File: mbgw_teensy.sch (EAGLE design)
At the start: 39 parts, among them IC1 MAX481CSA, Q1 MOSFET-N2N7002, Q2 MOSFET-N2N7002, Q3 MOSFET-N2N7002

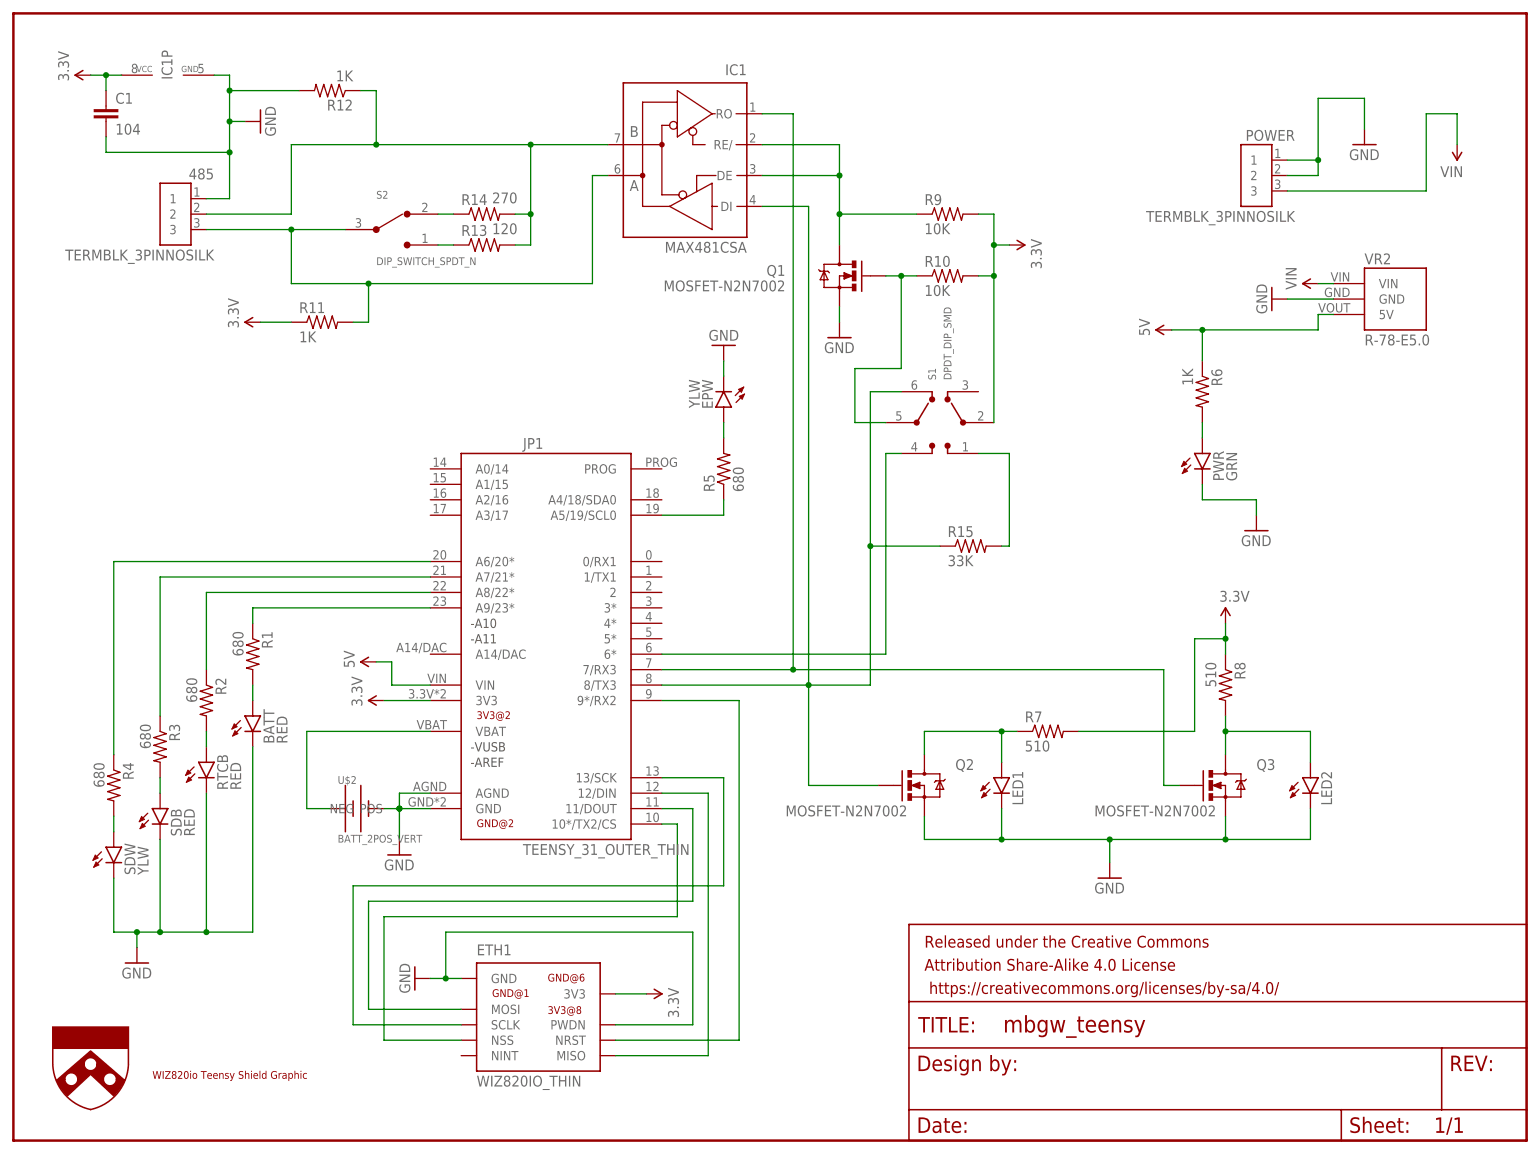
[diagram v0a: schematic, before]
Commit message: 3/16/17, board with software switches for term resistor and tx/p6 control
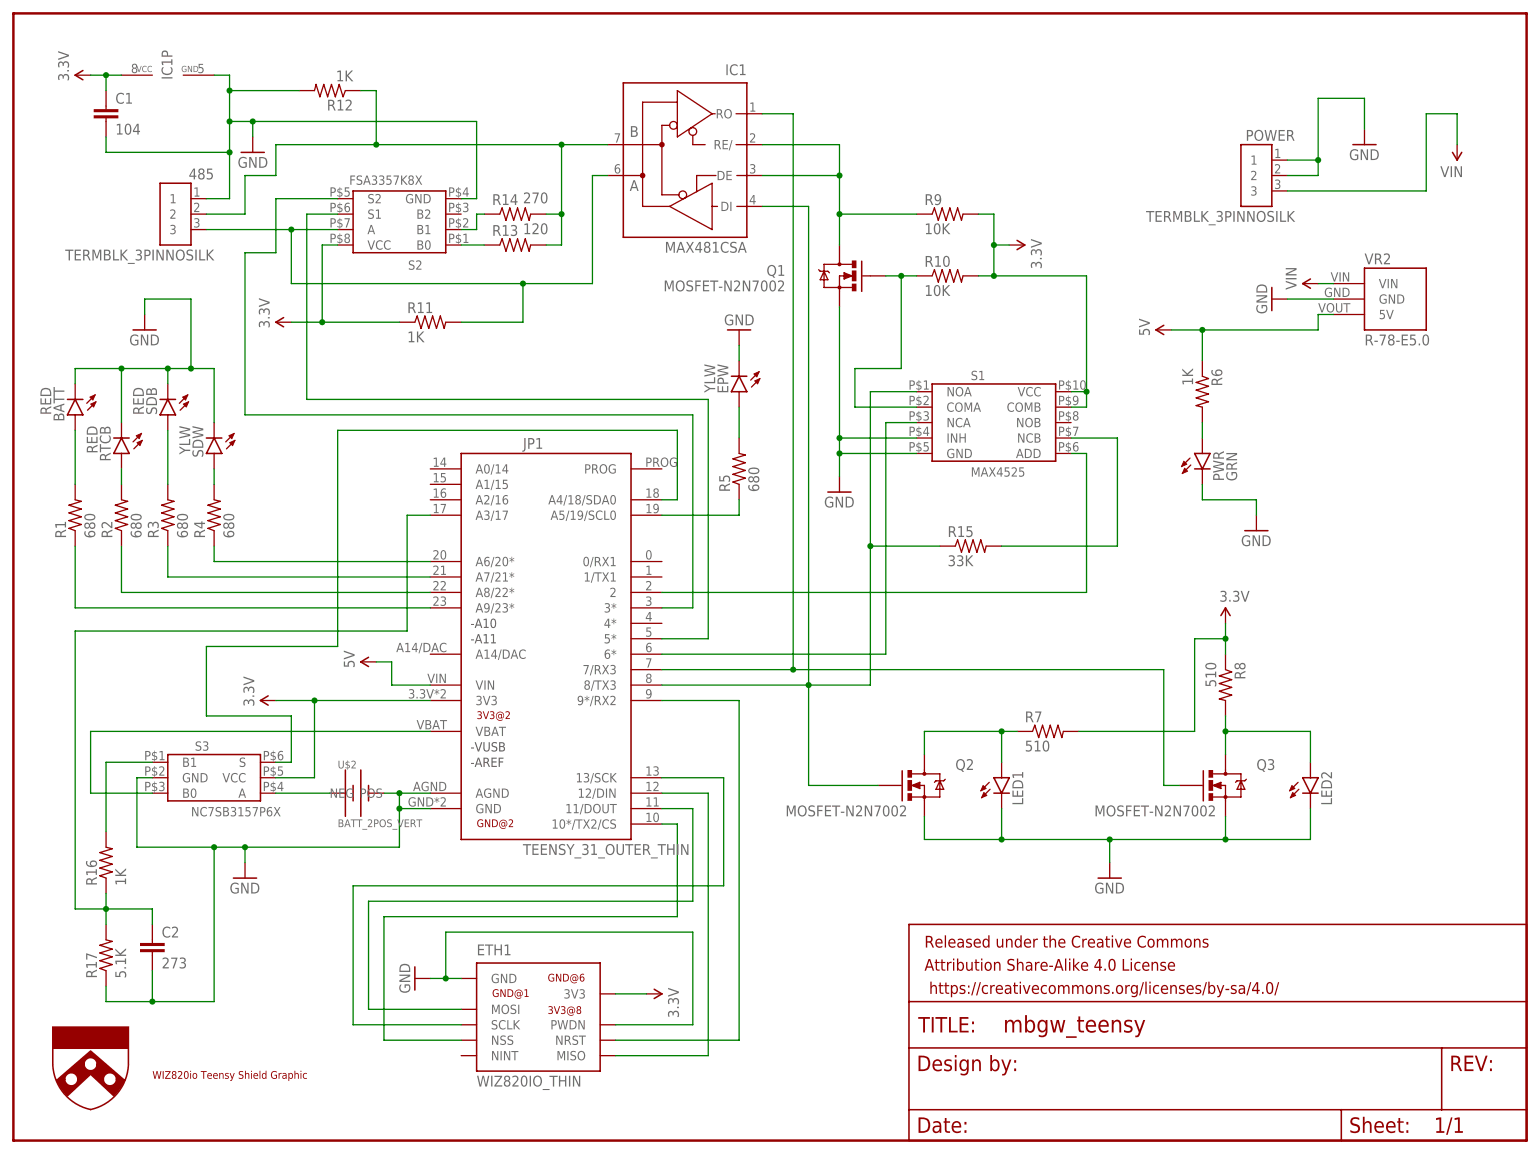
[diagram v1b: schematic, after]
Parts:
- added C2: 273, SparkFun-Capacitors:CAP0603-CAP
- added R16: 1K, SparkFun-Resistors:RESISTOR0603
- added R17: 5.1K, SparkFun-Resistors:RESISTOR0603
- added S3: NC7SB3157P6X, UPenn:NC7SB3157P6X
- S1: value DPDT_DIP_SMD -> MAX4525; device UPenn:DPDT_DIP_SMD -> UPenn:MAX4525
- S2: value DIP_SWITCH_SPDT_N -> FSA3357K8X; device UPenn:DIP_SWITCH_SPDT_N -> UPenn:FSA3357K8X
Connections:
- new net N$30: R14.1, S2.B1
- new net N$31: JP1.3*, S2.S2
- new net N$32: JP1.2, S1.ADD
- new net N$33: JP1.VBAT, S3.B0
- new net N$35: C2.1, JP1.A3/17, R16.1, R17.2
- new net N$37: R16.2, S3.B1
- new net N$38: JP1.A4/18/SDA0, S3.S
- net 3.3V: now also S1.COMB, S1.VCC, S2.VCC, S3.VCC; no longer S1.<2
- net GND: now also C2.2, R17.1, S1.GND, S1.INH, S2.GND, S3.GND
- net N$1: now also R15.2, S1.NCB; no longer R14.1, S2.2
- net N$12: now also S2.B0; no longer S2.1
- net N$15: now also JP1.5*, S2.S1; no longer R15.2, S1.<1
- net N$17: now also S1.NOA; no longer S1.6>
- net N$2: now also S1.NCA; no longer S1.4>
- net N$25: now also S2.A; no longer S2.3
- net N$26: now also S1.COMA; no longer S1.5>
- net N$3: now also S3.A; no longer JP1.VBAT
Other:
- moved on the sheet: BATT, EPW, R1, R11, R13, R14, R2, R3, R4, R5, RTCB, SDB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

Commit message: 3/20/17, continue adjusting for stretched board
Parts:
- added MEM1: RM25C512CSOIC, UPenn:RM25C512CSOIC
- added R18: 180, SparkFun-Resistors:RESISTOR0603
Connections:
- new net N$34: R18.1, S2.B2
- net 3.3V: now also MEM1.!HOLD!, MEM1.!WP!, MEM1.VCC
- net GND: now also MEM1.GND
- net N$13: now also R18.2
- net N$6: now also MEM1.SDI
- net N$7: now also MEM1.SDO
- net N$8: now also MEM1.SCK
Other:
- moved on the sheet: LED1, LED2, Q2, Q3, R13, R14, R15, R7, S1

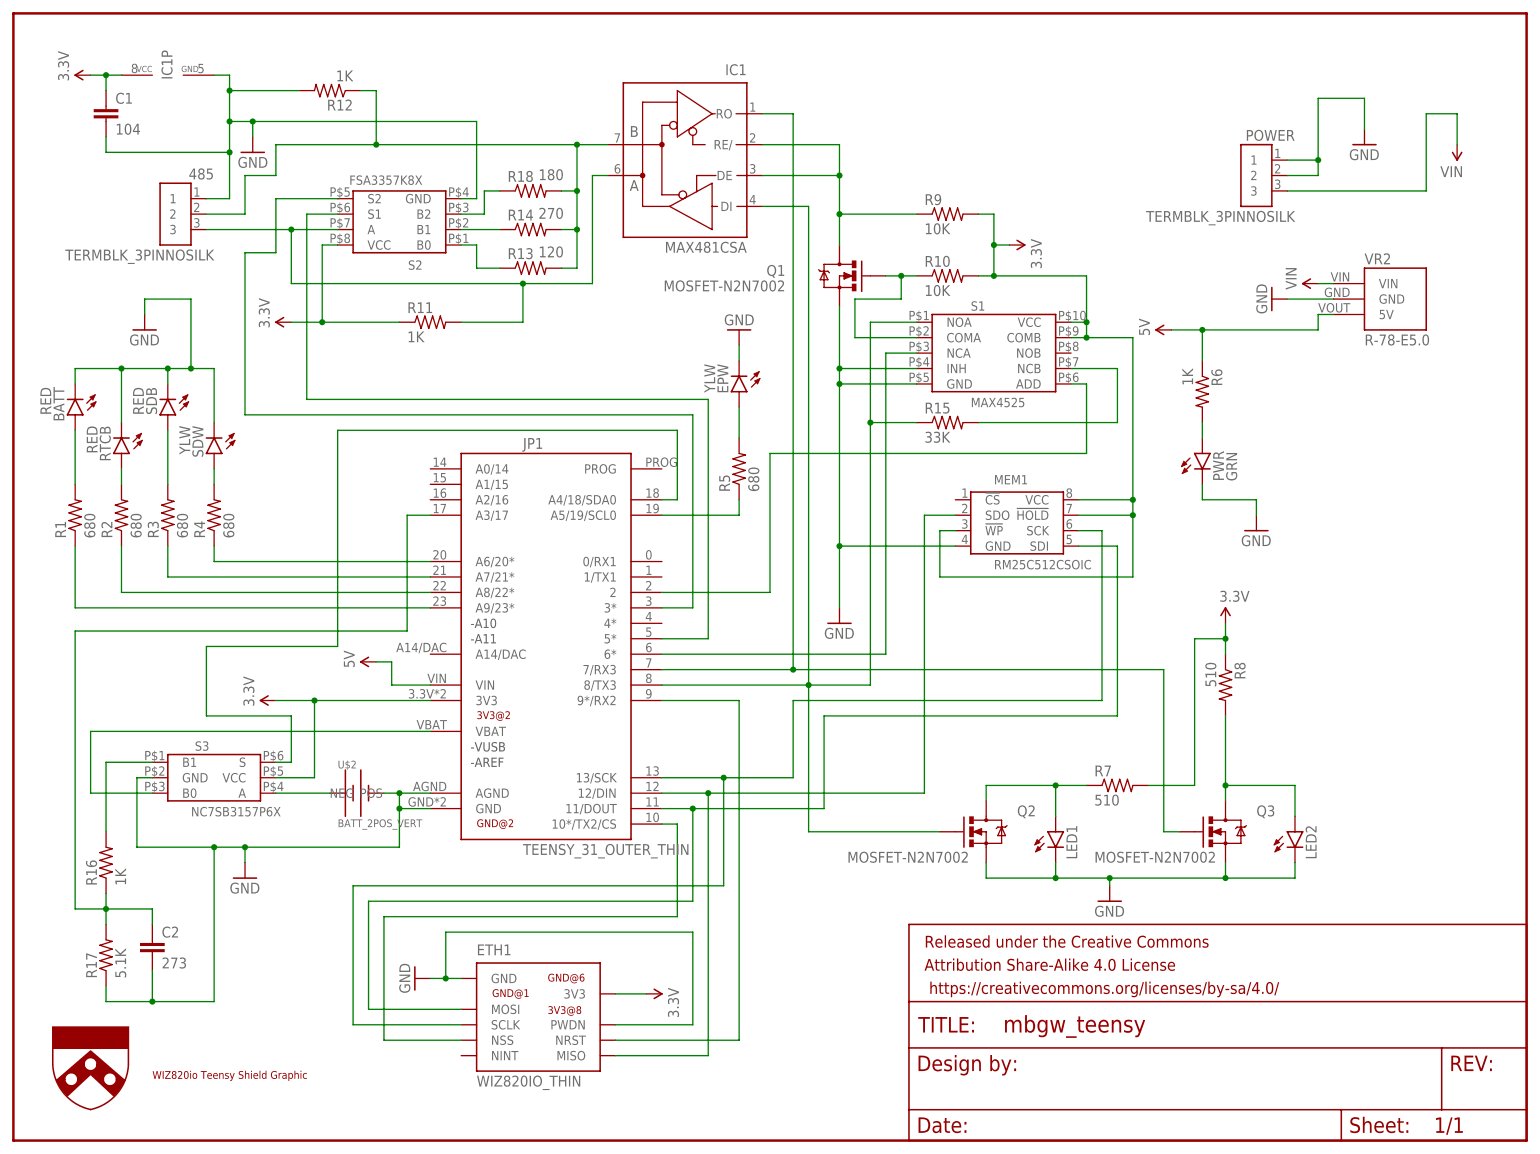
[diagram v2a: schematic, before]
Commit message: 3/21/17, all chips connected, make sure everything visible
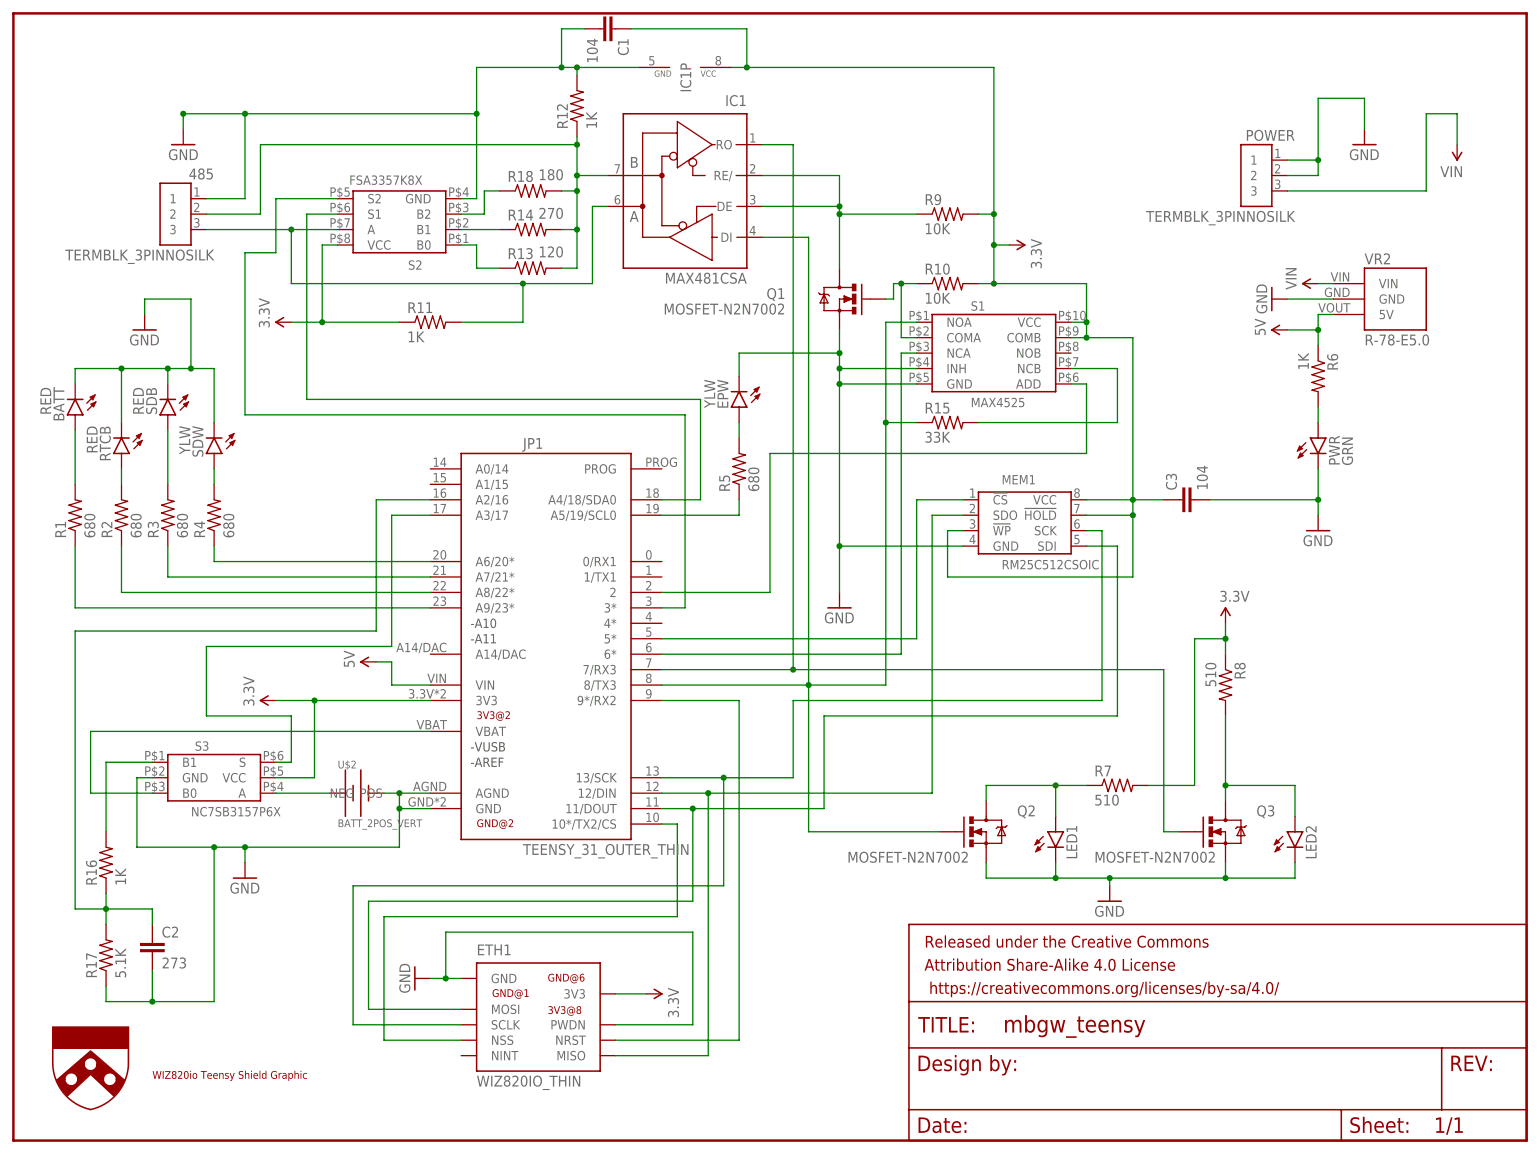
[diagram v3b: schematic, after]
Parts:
- added C3: 104, SparkFun-Capacitors:CAP0603-CAP
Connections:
- new net N$36: JP1.5*, MEM1.!CS!
- net 3.3V: now also C3.1
- net GND: now also C3.2
- net N$15: now also JP1.A4/18/SDA0; no longer JP1.5*
- net N$35: now also JP1.A2/16; no longer JP1.A3/17
- net N$38: now also JP1.A3/17; no longer JP1.A4/18/SDA0
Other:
- moved on the sheet: C1, EPW, IC1, IC1P, MEM1, PWR, Q1, R10, R12, R6

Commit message: 3/23/17, added BOM
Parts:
- RX, TX: value (none) -> YLW
- renumbered LED1 to TX, LED2 to RX
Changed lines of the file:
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@@
 <setting verticaltext="up"/>
 </settings>
-<grid distance="0.05" unitdist="inch" unit="inch" style="lines" multiple="1" display="yes" altdistance="0.05" altunitdist="inch" altunit="inch"/>
+<grid distance="0.1" unitdist="inch" unit="inch" style="lines" multiple="1" display="no" altdistance="0.01" altunitdist="inch" altunit="inch"/>
 <layers>
 <layer number="1" name="Top" color="4" fill="1" visible="no" active="no"/>
@@
 <part name="R14" library="SparkFun-Resistors" deviceset="RESISTOR" device="0603" value="270"/>
 <part name="C1" library="SparkFun-Capacitors" deviceset="CAP" device="0603-CAP" value="104"/>
-<part name="LED1" library="SparkFun-LED" deviceset="LED" device="0603"/>
-<part name="LED2" library="SparkFun-LED" deviceset="LED" device="0603"/>
+<part name="TX" library="SparkFun-LED" deviceset="LED" device="0603" value="YLW"/>
+<part name="RX" library="SparkFun-LED" deviceset="LED" device="0603" value="YLW"/>
 <part name="IC1" library="maxim" deviceset="MAX481CSA" device=""/>
 <part name="Q2" library="UPenn" deviceset="MOSFET-N" device="2N7002"/>
@@
 </instance>
 <instance part="C1" gate="G$1" x="96.52" y="182.88" rot="R270"/>
-<instance part="LED1" gate="G$1" x="171.45" y="50.8"/>
-<instance part="LED2" gate="G$1" x="210.82" y="50.8"/>
+<instance part="TX" gate="G$1" x="171.45" y="50.8"/>
+<instance part="RX" gate="G$1" x="210.82" y="50.8"/>
 <instance part="IC1" gate="G$1" x="110.49" y="156.21" rot="MR0"/>
 <instance part="Q2" gate="G$1" x="160.02" y="50.8" smashed="yes">
@@
 <pinref part="Q2" gate="G$1" pin="S"/>
 <wire x1="160.02" y1="45.72" x2="160.02" y2="43.18" width="0.1524" layer="91"/>
-<pinref part="LED2" gate="G$1" pin="C"/>
+<pinref part="RX" gate="G$1" pin="C"/>
 <wire x1="160.02" y1="43.18" x2="171.45" y2="43.18" width="0.1524" layer="91"/>
 <wire x1="171.45" y1="43.18" x2="180.34" y2="43.18" width="0.1524" layer="91"/>
@@
 <wire x1="199.39" y1="43.18" x2="210.82" y2="43.18" width="0.1524" layer="91"/>
 <wire x1="210.82" y1="43.18" x2="210.82" y2="45.72" width="0.1524" layer="91"/>
-<pinref part="LED1" gate="G$1" pin="C"/>
+<pinref part="TX" gate="G$1" pin="C"/>
 <wire x1="171.45" y1="45.72" x2="171.45" y2="43.18" width="0.1524" layer="91"/>
 <junction x="171.45" y="43.18"/>
@@
 <net name="N$28" class="0">
 <segment>
-<pinref part="LED2" gate="G$1" pin="A"/>
+<pinref part="RX" gate="G$1" pin="A"/>
 <pinref part="R8" gate="G$1" pin="2"/>
 <wire x1="199.39" y1="69.85" x2="199.39" y2="58.42" width="0.1524" layer="91"/>
@@
 <pinref part="R7" gate="G$1" pin="1"/>
 <wire x1="160.02" y1="58.42" x2="171.45" y2="58.42" width="0.1524" layer="91"/>
-<pinref part="LED1" gate="G$1" pin="A"/>
+<pinref part="TX" gate="G$1" pin="A"/>
 <wire x1="171.45" y1="58.42" x2="176.53" y2="58.42" width="0.1524" layer="91"/>
 <wire x1="171.45" y1="53.34" x2="171.45" y2="58.42" width="0.1524" layer="91"/>

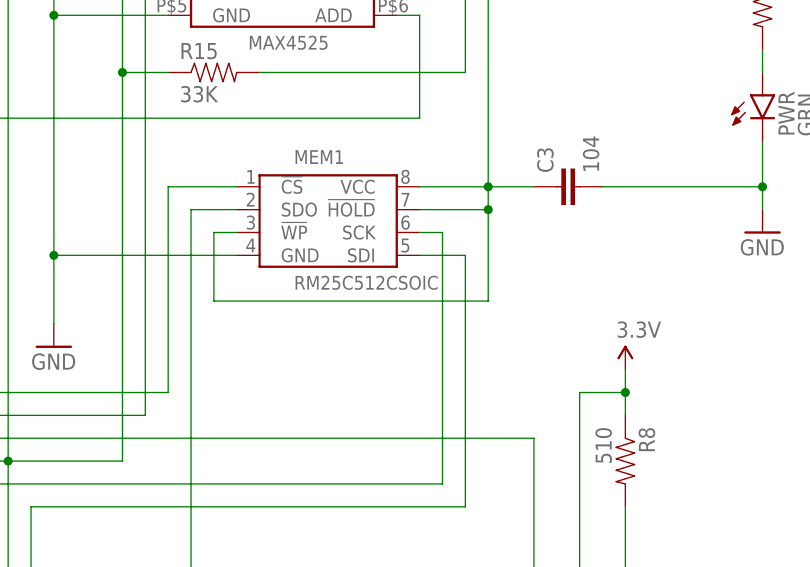
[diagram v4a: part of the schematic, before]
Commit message: 3/23/17, fram instead of eeprom memory
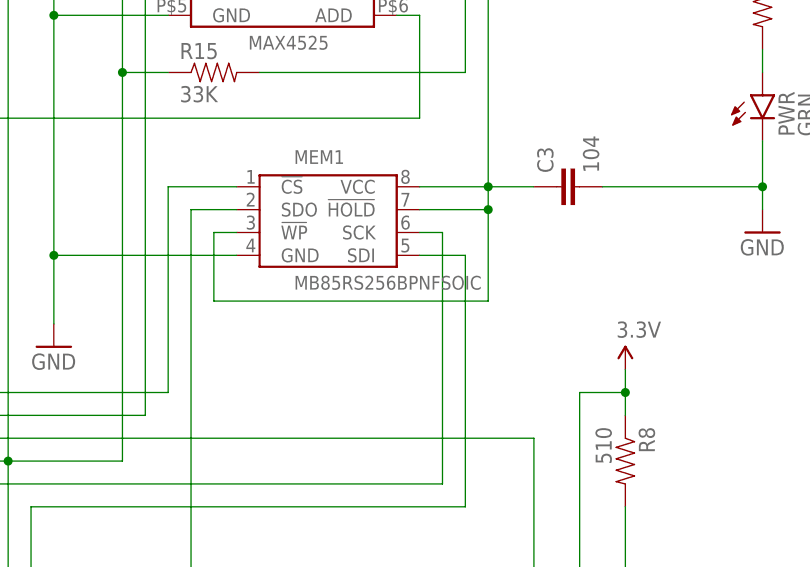
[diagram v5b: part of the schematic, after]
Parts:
- MEM1: value RM25C512CSOIC -> MB85RS256BPNFSOIC; device UPenn:RM25C512CSOIC -> UPenn:MB85RS256BPNFSOIC
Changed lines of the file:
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@@
 <setting verticaltext="up"/>
 </settings>
-<grid distance="0.1" unitdist="inch" unit="inch" style="lines" multiple="1" display="no" altdistance="0.01" altunitdist="inch" altunit="inch"/>
+<grid distance="0.05" unitdist="inch" unit="inch" style="lines" multiple="1" display="yes" altdistance="0.05" altunitdist="inch" altunit="inch"/>
 <layers>
 <layer number="1" name="Top" color="4" fill="1" visible="no" active="no"/>
@@
 <part name="R17" library="SparkFun-Resistors" deviceset="RESISTOR" device="0603" value="5.1K"/>
 <part name="C2" library="SparkFun-Capacitors" deviceset="CAP" device="0603-CAP" value="273"/>
-<part name="MEM1" library="UPenn" deviceset="RM25C512C" device="SOIC"/>
+<part name="MEM1" library="UPenn" deviceset="MB85RS256BPNF" device="SOIC"/>
 <part name="R18" library="SparkFun-Resistors" deviceset="RESISTOR" device="0603" value="180"/>
 <part name="C3" library="SparkFun-Capacitors" deviceset="CAP" device="0603-CAP" value="104"/>
